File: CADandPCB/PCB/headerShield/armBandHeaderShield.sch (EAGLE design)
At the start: 11 parts

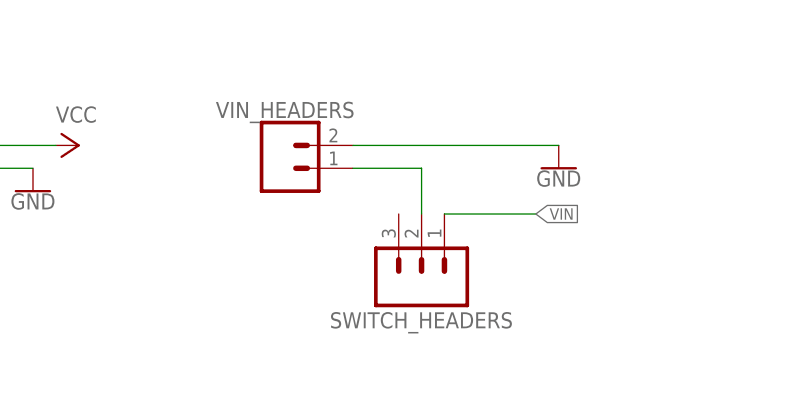
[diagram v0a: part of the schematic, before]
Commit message: Offset swtich headers.
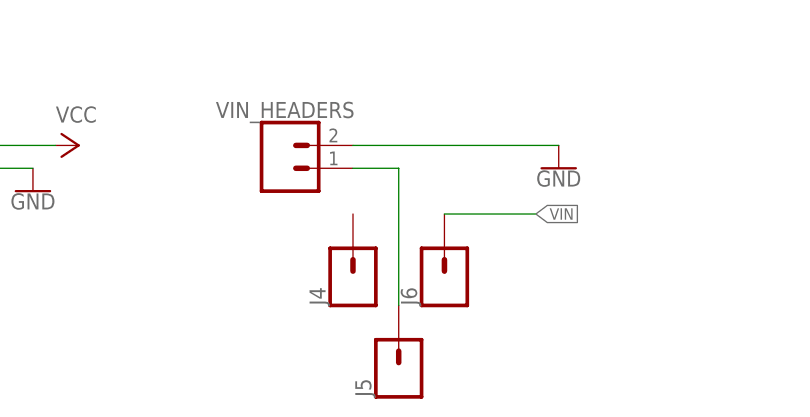
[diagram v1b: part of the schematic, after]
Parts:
- removed SWITCH_HEADERS: 455-1750-1-ND, SparkFun-Connectors:CONN_03
- added J4, J5, J6: (no value), SparkFun-Connectors:CONN_01
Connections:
- net N$1: now also J5.1; no longer SWITCH_HEADERS.2
- net VIN: now also J6.1; no longer SWITCH_HEADERS.1
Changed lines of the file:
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@@
 <part name="GND17" library="SparkFun-PowerSymbols" deviceset="GND" device=""/>
 <part name="GND19" library="SparkFun-Aesthetics" deviceset="GND" device=""/>
-<part name="SWITCH_HEADERS" library="SparkFun-Connectors" deviceset="CONN_03" device="" value="455-1750-1-ND"/>
 <part name="P+2" library="supply1" library_urn="urn:adsk.eagle:library:371" deviceset="VCC" device=""/>
 <part name="J1" library="SparkFun-Connectors" deviceset="CONN_04" device=""/>
@@
 <part name="2KOHM_R" library="SparkFun-Connectors" deviceset="CONN_01" device=""/>
 <part name="FROM_TX" library="SparkFun-Connectors" deviceset="CONN_01" device=""/>
+<part name="J4" library="SparkFun-Connectors" deviceset="CONN_01" device=""/>
+<part name="J5" library="SparkFun-Connectors" deviceset="CONN_01" device=""/>
+<part name="J6" library="SparkFun-Connectors" deviceset="CONN_01" device=""/>
 </parts>
 <sheets>
@@
 <attribute name="VALUE" x="238.76" y="43.18" size="1.778" layer="96"/>
 </instance>
-<instance part="SWITCH_HEADERS" gate="J$1" x="180.34" y="-10.16" smashed="yes" rot="R90">
-<attribute name="NAME" x="190.5" y="-13.462" size="1.778" layer="95" font="vector" rot="R180"/>
-</instance>
 <instance part="P+2" gate="VCC" x="231.14" y="45.72" smashed="yes" rot="R270">
 <attribute name="VALUE" x="231.14" y="43.18" size="1.778" layer="96"/>
@@
 <attribute name="VALUE" x="152.146" y="93.98" size="1.778" layer="96" font="vector" rot="R90"/>
 <attribute name="NAME" x="160.528" y="95.758" size="1.778" layer="95" font="vector" rot="R180"/>
+</instance>
+<instance part="J4" gate="G$1" x="172.72" y="-10.16" smashed="yes" rot="R90">
+<attribute name="VALUE" x="177.546" y="-12.7" size="1.778" layer="96" font="vector" rot="R90"/>
+<attribute name="NAME" x="169.672" y="-12.7" size="1.778" layer="95" font="vector" rot="R90"/>
+</instance>
+<instance part="J5" gate="G$1" x="177.8" y="-20.32" smashed="yes" rot="R90">
+<attribute name="VALUE" x="182.626" y="-22.86" size="1.778" layer="96" font="vector" rot="R90"/>
+<attribute name="NAME" x="174.752" y="-22.86" size="1.778" layer="95" font="vector" rot="R90"/>
+</instance>
+<instance part="J6" gate="G$1" x="182.88" y="-10.16" smashed="yes" rot="R90">
+<attribute name="VALUE" x="187.706" y="-12.7" size="1.778" layer="96" font="vector" rot="R90"/>
+<attribute name="NAME" x="179.832" y="-12.7" size="1.778" layer="95" font="vector" rot="R90"/>
 </instance>
 </instances>
@@
 <wire x1="182.88" y1="-2.54" x2="193.04" y2="-2.54" width="0.1524" layer="91"/>
 <label x="193.04" y="-2.54" size="1.27" layer="95" xref="yes"/>
-<pinref part="SWITCH_HEADERS" gate="J$1" pin="1"/>
+<pinref part="J6" gate="G$1" pin="1"/>
 </segment>
 </net>
@@
 <segment>
 <pinref part="VIN_HEADERS" gate="G$1" pin="1"/>
-<pinref part="SWITCH_HEADERS" gate="J$1" pin="2"/>
-<wire x1="172.72" y1="2.54" x2="180.34" y2="2.54" width="0.1524" layer="91"/>
-<wire x1="180.34" y1="2.54" x2="180.34" y2="-2.54" width="0.1524" layer="91"/>
-</segment>
-</net>
+<wire x1="172.72" y1="2.54" x2="177.8" y2="2.54" width="0.1524" layer="91"/>
+<wire x1="177.8" y1="2.54" x2="177.8" y2="-12.7" width="0.1524" layer="91"/>
+<pinref part="J5" gate="G$1" pin="1"/>
+</segment>
+</net>

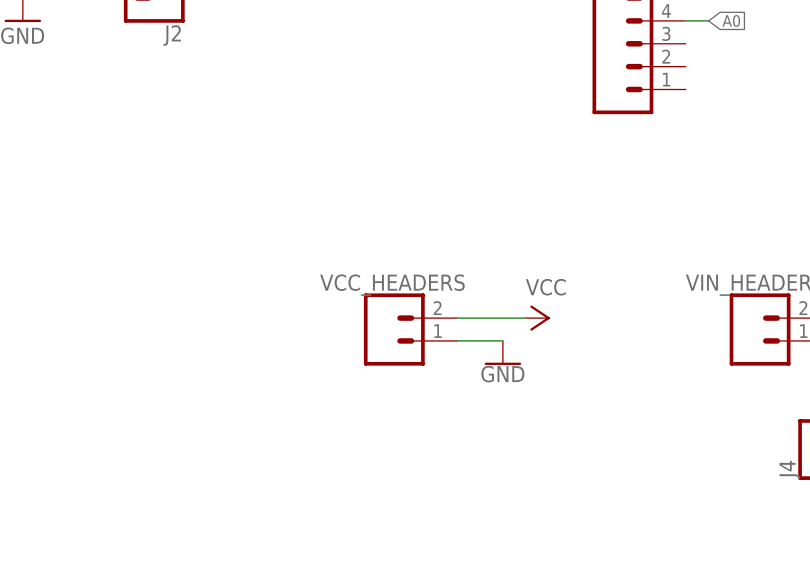
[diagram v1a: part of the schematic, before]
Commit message: Commit Gerber files and final rev 1 for the header version of board.
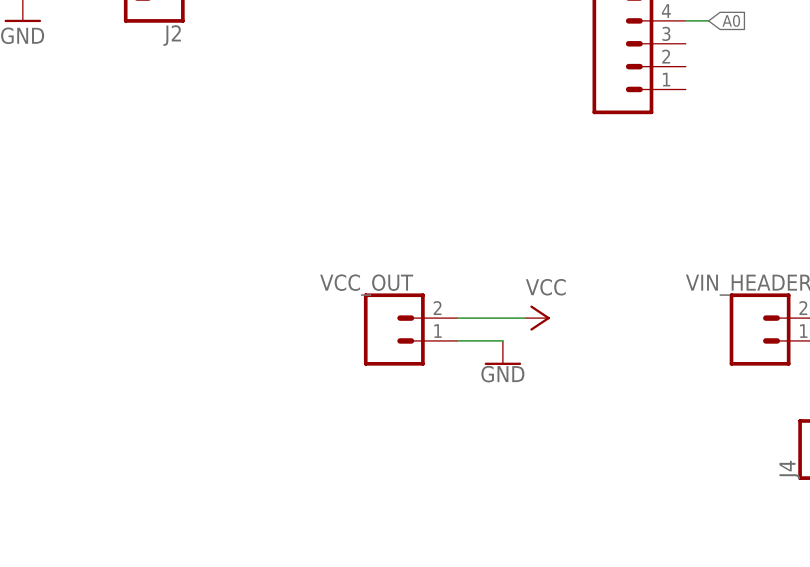
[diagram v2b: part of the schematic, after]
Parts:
- removed VCC_HEADERS: (no value), SparkFun-Connectors:CONN_02
- added VCC_OUT: (no value), SparkFun-Connectors:CONN_02PTH3
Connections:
- net GND: now also VCC_OUT.1; no longer VCC_HEADERS.1
- net VCC: now also VCC_OUT.2; no longer VCC_HEADERS.2
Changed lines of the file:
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@@
 <?xml version="1.0" encoding="utf-8"?>
 <!DOCTYPE eagle SYSTEM "eagle.dtd">
-<eagle version="9.3.0">
+<eagle version="9.3.1">
 <drawing>
 <settings>
@@
 <part name="P+4" library="supply1" library_urn="urn:adsk.eagle:library:371" deviceset="VCC" device=""/>
 <part name="GND15" library="SparkFun-PowerSymbols" deviceset="GND" device=""/>
-<part name="VCC_HEADERS" library="SparkFun-Connectors" deviceset="CONN_02" device=""/>
 <part name="P+5" library="supply1" library_urn="urn:adsk.eagle:library:371" deviceset="VCC" device=""/>
 <part name="GND16" library="SparkFun-PowerSymbols" deviceset="GND" device=""/>
@@
 <part name="J5" library="SparkFun-Connectors" deviceset="CONN_01" device=""/>
 <part name="J6" library="SparkFun-Connectors" deviceset="CONN_01" device=""/>
+<part name="VCC_OUT" library="SparkFun-Connectors" deviceset="CONN_02" device="PTH3"/>
 </parts>
 <sheets>
@@
 <attribute name="VALUE" x="187.96" y="103.886" size="1.778" layer="96" align="top-center"/>
 </instance>
-<instance part="VCC_HEADERS" gate="G$1" x="124.46" y="2.54" smashed="yes">
-<attribute name="VALUE" x="121.92" y="-2.286" size="1.778" layer="96" font="vector"/>
-<attribute name="NAME" x="116.84" y="8.128" size="1.778" layer="95" font="vector"/>
-</instance>
 <instance part="P+5" gate="VCC" x="142.24" y="5.08" smashed="yes" rot="R270">
 <attribute name="VALUE" x="139.7" y="7.62" size="1.778" layer="96"/>
@@
 <attribute name="VALUE" x="187.706" y="-12.7" size="1.778" layer="96" font="vector" rot="R90"/>
 <attribute name="NAME" x="179.832" y="-12.7" size="1.778" layer="95" font="vector" rot="R90"/>
+</instance>
+<instance part="VCC_OUT" gate="G$1" x="124.46" y="2.54" smashed="yes">
+<attribute name="VALUE" x="121.92" y="-2.286" size="1.778" layer="96" font="vector"/>
+<attribute name="NAME" x="116.84" y="8.128" size="1.778" layer="95" font="vector"/>
 </instance>
 </instances>
@@
 <segment>
 <pinref part="GND16" gate="1" pin="GND"/>
-<pinref part="VCC_HEADERS" gate="G$1" pin="1"/>
 <wire x1="137.16" y1="2.54" x2="132.08" y2="2.54" width="0.1524" layer="91"/>
+<pinref part="VCC_OUT" gate="G$1" pin="1"/>
 </segment>
 <segment>
@@
 </segment>
 <segment>
-<pinref part="VCC_HEADERS" gate="G$1" pin="2"/>
 <pinref part="P+5" gate="VCC" pin="VCC"/>
 <wire x1="132.08" y1="5.08" x2="139.7" y2="5.08" width="0.1524" layer="91"/>
-</segment>
-<segment>
+<pinref part="VCC_OUT" gate="G$1" pin="2"/>
+</segment>
+<segment>
